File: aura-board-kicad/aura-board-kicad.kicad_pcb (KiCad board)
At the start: 2 copper layers, 75.6 x 53.3 mm, 16 parts, among them J1 Main Power, J2 PWM Outputs, J3 BB-UART0, J4 Attopilot, J5 GPS, J6 SBUS, J7 Telemetry, U1 TSR2-2450, U2 PocketBeagle, U3 Teensy-3.2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

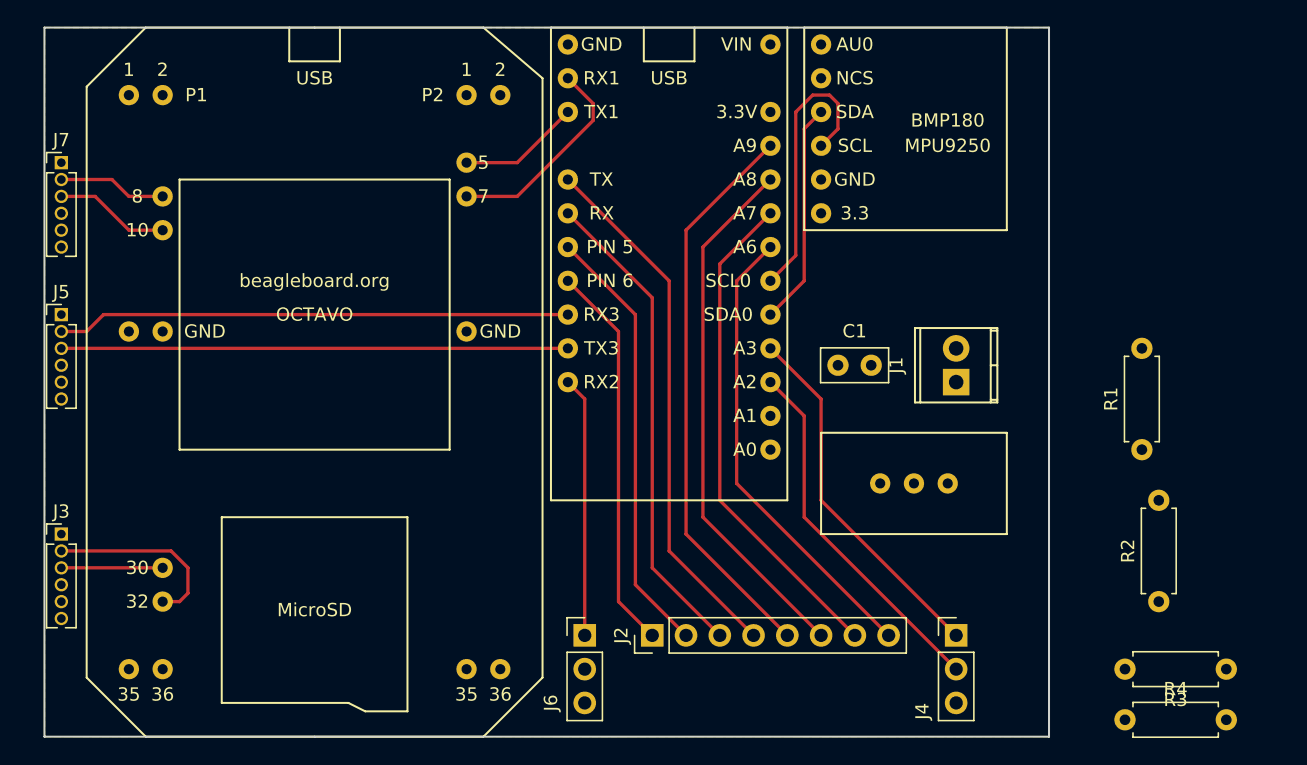
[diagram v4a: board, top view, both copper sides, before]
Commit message: More trace routing and tweaking.
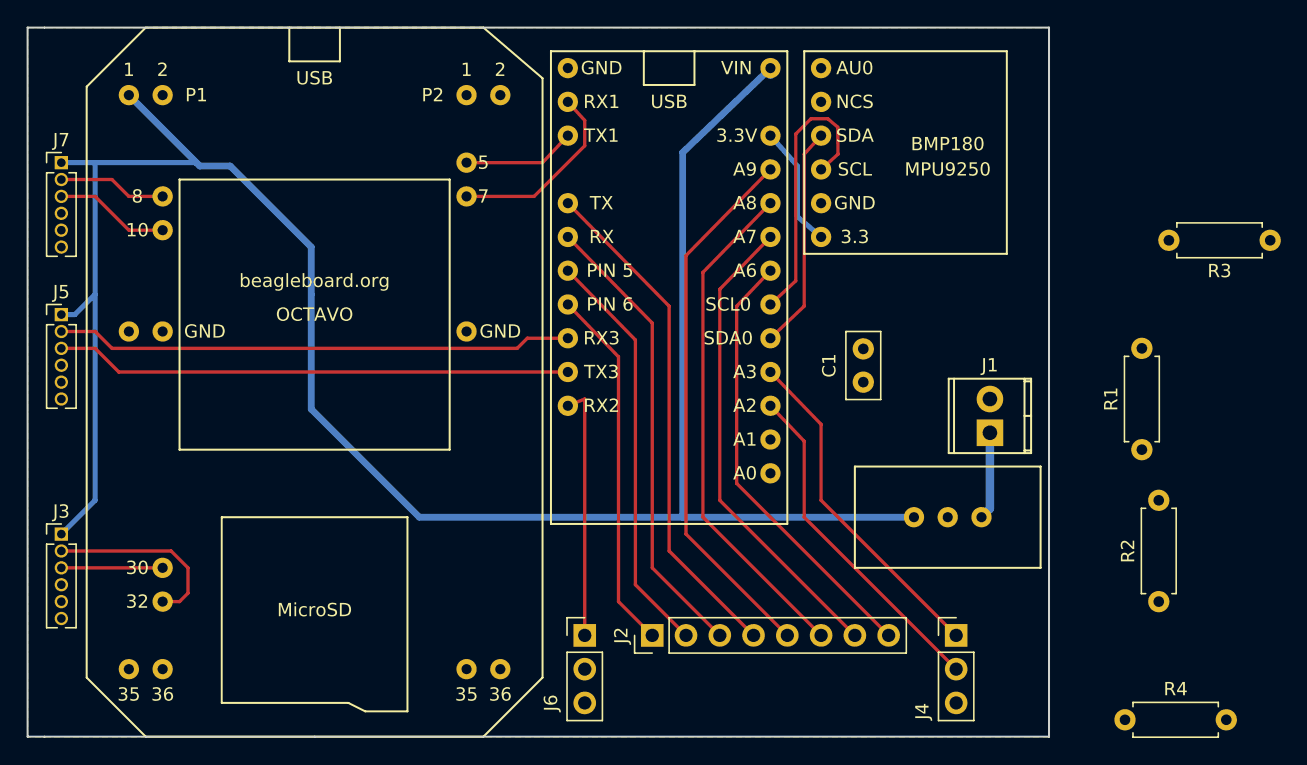
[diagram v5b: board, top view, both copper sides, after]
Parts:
- moved R3 32.4 mm to (121.4, 65.5)
- moved J1 4.58 mm to (100.3, 80.0)
- moved U1 3.59 mm to (97.2, 90.2)
- moved C1 2.29 mm to (90.8, 76.2), turned to 90 degrees
- moved U4 1.78 mm to (94.0, 66.5)
- moved U3 1.78 mm to (76.2, 51.3)
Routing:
- net +5V: track 0.00 -> 158.9 mm
- net +3V3: track 0.00 -> 9.21 mm
- net VDD: track 0.00 -> 6.61 mm
- net /PWM4: track 40.1 -> 38.3 mm
- net /PWM3: track 36.5 -> 34.7 mm
- net /PWM5: track 42.6 -> 40.8 mm
- net /PWM2: track 32.9 -> 31.1 mm
- net /PWM6: track 40.1 -> 38.3 mm
- net /PWM7: track 37.5 -> 35.7 mm
- net /PWM1: track 29.3 -> 27.5 mm
- net /ATTO_VOLTS: track 27.4 -> 25.6 mm
- net /PWM8: track 35.0 -> 33.2 mm
- net /ATTO_AMPS: track 27.4 -> 25.6 mm
- net /UART1_RX: track 15.9 -> 14.3 mm
- net /GPS_TX: track 38.1 -> 38.8 mm
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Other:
- board size 75.6 x 53.3 mm -> 76.8 x 53.3 mm

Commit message: More trace routing. Position resistors for voltage divider/sending circuits. Add mounting holes (3mm).
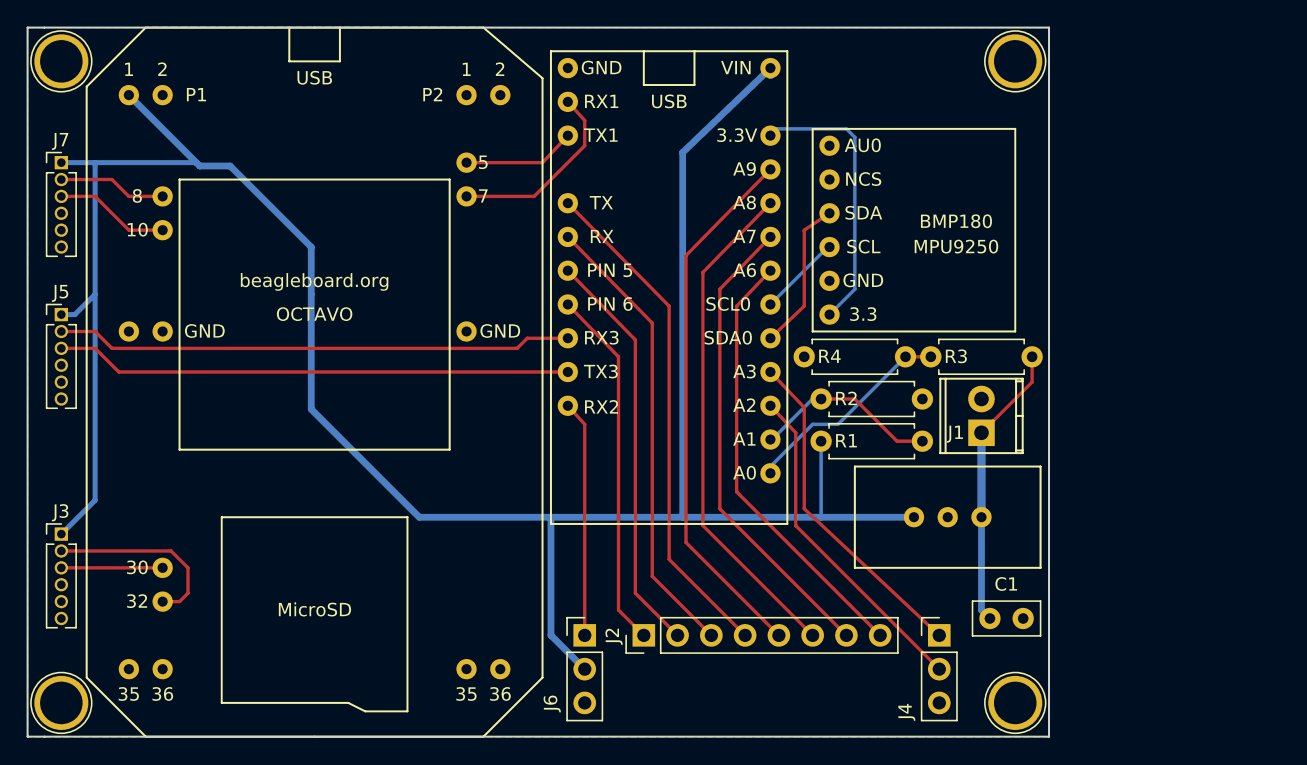
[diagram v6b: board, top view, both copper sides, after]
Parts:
- added REF**: 1pin, Connectors:1pin, F.Cu at (30.5, 52.1)
- added REF**: 1pin, Connectors:1pin, F.Cu at (30.5, 100.3)
- added REF**: 1pin, Connectors:1pin, F.Cu at (102.2, 100.3)
- added REF**: 1pin, Connectors:1pin, F.Cu at (102.2, 52.1)
- moved R4 36.4 mm to (86.4, 74.3)
- moved R3 27.0 mm to (95.9, 74.3), turned to 0 degrees
- moved R2 23.4 mm to (95.2, 77.5), turned to 180 degrees
- moved C1 20.2 mm to (100.3, 94.0), turned to 0 degrees
- moved R1 16.5 mm to (95.2, 80.6), turned to 180 degrees
- moved U4 5.88 mm to (94.6, 72.4)
- moved J4 1.27 mm to (96.5, 95.2)
- moved J1 0.64 mm to (99.7, 80.0)
- moved J2 0.64 mm to (74.3, 95.2)
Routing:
- net +5V: track 158.9 -> 176.5 mm
- net /MAIN_VCC: track 0.00 -> 16.0 mm
- net /I2C0_SCL: track 21.3 -> 6.23 mm
- net VDD: track 6.61 -> 21.5 mm
- net /AVIONICS_VCC: track 0.00 -> 14.0 mm
- net +3V3: track 9.21 -> 20.9 mm
- net /I2C0_SDA: track 16.8 -> 11.5 mm
- net /SBUS_RX: track 19.1 -> 17.8 mm
- net /ATTO_AMPS: track 25.6 -> 25.0 mm

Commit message: Add a +5V power bus plane on the top layer.
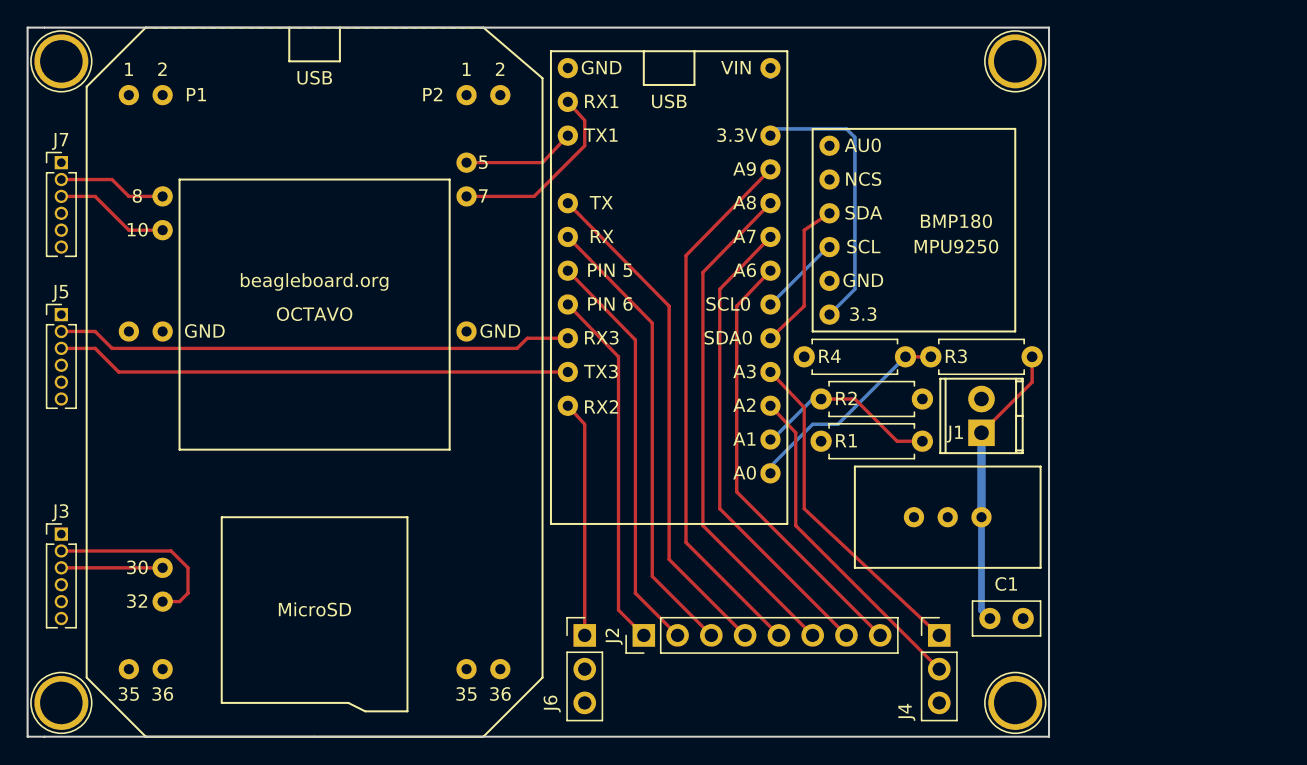
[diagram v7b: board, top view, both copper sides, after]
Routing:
- net +5V: track 176.5 -> 1.02 mm
- added copper zone on F.Cu, net +5V

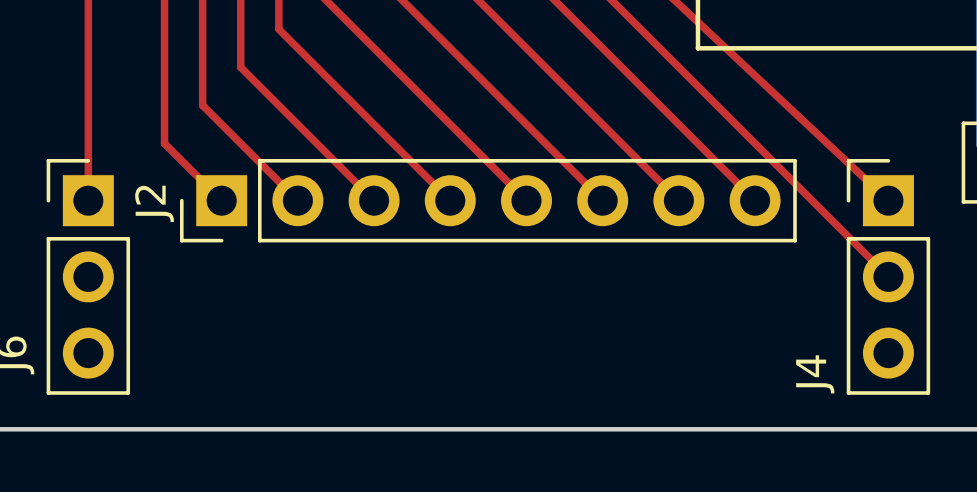
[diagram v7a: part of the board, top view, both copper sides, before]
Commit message: Add pin headers to complete pwm header block.
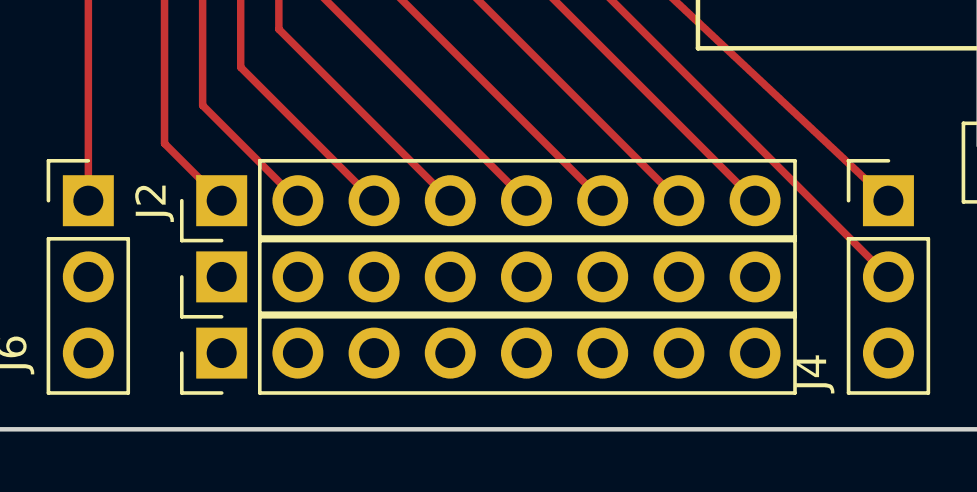
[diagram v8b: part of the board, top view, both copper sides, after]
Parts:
- added ?: 1x08, Pin_Headers:Pin_Header_Straight_1x08_Pitch2.54mm, F.Cu at (74.3, 97.8)
- added ?: 1x08, Pin_Headers:Pin_Header_Straight_1x08_Pitch2.54mm, F.Cu at (74.3, 100.3)
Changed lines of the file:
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@@
     (tracks 92)
     (zones 0)
-    (modules 20)
+    (modules 22)
     (nets 33)
   )
@@
   (layers
     (0 F.Cu signal)
-    (31 B.Cu signal hide)
+    (31 B.Cu signal)
     (32 B.Adhes user)
     (33 F.Adhes user)
@@
     (fp_line (start 1.8 19.55) (end 1.8 -1.8) (layer F.CrtYd) (width 0.05))
     (fp_line (start 1.8 -1.8) (end -1.8 -1.8) (layer F.CrtYd) (width 0.05))
-    (fp_text user %R (at 0 8.89 180) (layer F.Fab)
+    (fp_text user %R (at 2.54 -0.635 180) (layer F.Fab)
       (effects (font (size 1 1) (thickness 0.15)))
     )
@@
     (fp_line (start 1.8 6.85) (end 1.8 -1.8) (layer F.CrtYd) (width 0.05))
     (fp_line (start 1.8 -1.8) (end -1.8 -1.8) (layer F.CrtYd) (width 0.05))
-    (fp_text user %R (at 0 2.54 90) (layer F.Fab)
+    (fp_text user %R (at -1.905 2.54 90) (layer F.Fab)
       (effects (font (size 1 1) (thickness 0.15)))
     )
@@
     (pad 1 thru_hole circle (at 0 0) (size 4.064 4.064) (drill 3.2) (layers *.Cu *.Mask))
   )
+  (module Pin_Headers:Pin_Header_Straight_1x08_Pitch2.54mm (layer F.Cu)
+    (at 74.295 97.79 90)
+    (descr "Through hole straight pin header, 1x08, 2.54mm pitch, single row")
+    (tags "Through hole pin header THT 1x08 2.54mm single row")
+    (fp_text reference "" (at 0 -2.33 90) (layer F.SilkS) hide
+      (effects (font (size 1 1) (thickness 0.15)))
+    )
+    (fp_text value 1x08 (at 0 20.11 90) (layer F.Fab) hide
+      (effects (font (size 1 1) (thickness 0.15)))
+    )
+    (fp_line (start -0.635 -1.27) (end 1.27 -1.27) (layer F.Fab) (width 0.1))
+    (fp_line (start 1.27 -1.27) (end 1.27 19.05) (layer F.Fab) (width 0.1))
+    (fp_line (start 1.27 19.05) (end -1.27 19.05) (layer F.Fab) (width 0.1))
+    (fp_line (start -1.27 19.05) (end -1.27 -0.635) (layer F.Fab) (width 0.1))
+    (fp_line (start -1.27 -0.635) (end -0.635 -1.27) (layer F.Fab) (width 0.1))
+    (fp_line (start -1.33 19.11) (end 1.33 19.11) (layer F.SilkS) (width 0.12))
+    (fp_line (start -1.33 1.27) (end -1.33 19.11) (layer F.SilkS) (width 0.12))
+    (fp_line (start 1.33 1.27) (end 1.33 19.11) (layer F.SilkS) (width 0.12))
+    (fp_line (start -1.33 1.27) (end 1.33 1.27) (layer F.SilkS) (width 0.12))
+    (fp_line (start -1.33 0) (end -1.33 -1.33) (layer F.SilkS) (width 0.12))
+    (fp_line (start -1.33 -1.33) (end 0 -1.33) (layer F.SilkS) (width 0.12))
+    (fp_line (start -1.8 -1.8) (end -1.8 19.55) (layer F.CrtYd) (width 0.05))
+    (fp_line (start -1.8 19.55) (end 1.8 19.55) (layer F.CrtYd) (width 0.05))
+    (fp_line (start 1.8 19.55) (end 1.8 -1.8) (layer F.CrtYd) (width 0.05))
+    (fp_line (start 1.8 -1.8) (end -1.8 -1.8) (layer F.CrtYd) (width 0.05))
+    (fp_text user %R (at 0 8.89 180) (layer F.Fab) hide
+      (effects (font (size 1 1) (thickness 0.15)))
+    )
+    (pad 1 thru_hole rect (at 0 0 90) (size 1.7 1.7) (drill 1) (layers *.Cu *.Mask))
+    (pad 2 thru_hole oval (at 0 2.54 90) (size 1.7 1.7) (drill 1) (layers *.Cu *.Mask))
+    (pad 3 thru_hole oval (at 0 5.08 90) (size 1.7 1.7) (drill 1) (layers *.Cu *.Mask))
+    (pad 4 thru_hole oval (at 0 7.62 90) (size 1.7 1.7) (drill 1) (layers *.Cu *.Mask))
+    (pad 5 thru_hole oval (at 0 10.16 90) (size 1.7 1.7) (drill 1) (layers *.Cu *.Mask))
+    (pad 6 thru_hole oval (at 0 12.7 90) (size 1.7 1.7) (drill 1) (layers *.Cu *.Mask))
+    (pad 7 thru_hole oval (at 0 15.24 90) (size 1.7 1.7) (drill 1) (layers *.Cu *.Mask))
+    (pad 8 thru_hole oval (at 0 17.78 90) (size 1.7 1.7) (drill 1) (layers *.Cu *.Mask))
+    (model ${KISYS3DMOD}/Pin_Headers.3dshapes/Pin_Header_Straight_1x08_Pitch2.54mm.wrl
+      (at (xyz 0 0 0))
+      (scale (xyz 1 1 1))
+      (rotate (xyz 0 0 0))
+    )
+  )
+  (module Pin_Headers:Pin_Header_Straight_1x08_Pitch2.54mm (layer F.Cu)
+    (at 74.295 100.33 90)
+    (descr "Through hole straight pin header, 1x08, 2.54mm pitch, single row")
+    (tags "Through hole pin header THT 1x08 2.54mm single row")
+    (fp_text reference "" (at 0 -2.33 90) (layer F.SilkS) hide
+      (effects (font (size 1 1) (thickness 0.15)))
+    )
+    (fp_text value 1x08 (at 0 20.11 90) (layer F.Fab) hide
+      (effects (font (size 1 1) (thickness 0.15)))
+    )
+    (fp_line (start -0.635 -1.27) (end 1.27 -1.27) (layer F.Fab) (width 0.1))
+    (fp_line (start 1.27 -1.27) (end 1.27 19.05) (layer F.Fab) (width 0.1))
+    (fp_line (start 1.27 19.05) (end -1.27 19.05) (layer F.Fab) (width 0.1))
+    (fp_line (start -1.27 19.05) (end -1.27 -0.635) (layer F.Fab) (width 0.1))
+    (fp_line (start -1.27 -0.635) (end -0.635 -1.27) (layer F.Fab) (width 0.1))
+    (fp_line (start -1.33 19.11) (end 1.33 19.11) (layer F.SilkS) (width 0.12))
+    (fp_line (start -1.33 1.27) (end -1.33 19.11) (layer F.SilkS) (width 0.12))
+    (fp_line (start 1.33 1.27) (end 1.33 19.11) (layer F.SilkS) (width 0.12))
+    (fp_line (start -1.33 1.27) (end 1.33 1.27) (layer F.SilkS) (width 0.12))
+    (fp_line (start -1.33 0) (end -1.33 -1.33) (layer F.SilkS) (width 0.12))
+    (fp_line (start -1.33 -1.33) (end 0 -1.33) (layer F.SilkS) (width 0.12))
+    (fp_line (start -1.8 -1.8) (end -1.8 19.55) (layer F.CrtYd) (width 0.05))
+    (fp_line (start -1.8 19.55) (end 1.8 19.55) (layer F.CrtYd) (width 0.05))
+    (fp_line (start 1.8 19.55) (end 1.8 -1.8) (layer F.CrtYd) (width 0.05))
+    (fp_line (start 1.8 -1.8) (end -1.8 -1.8) (layer F.CrtYd) (width 0.05))
+    (fp_text user %R (at 0 8.89 180) (layer F.Fab) hide
+      (effects (font (size 1 1) (thickness 0.15)))
+    )
+    (pad 1 thru_hole rect (at 0 0 90) (size 1.7 1.7) (drill 1) (layers *.Cu *.Mask))
+    (pad 2 thru_hole oval (at 0 2.54 90) (size 1.7 1.7) (drill 1) (layers *.Cu *.Mask))
+    (pad 3 thru_hole oval (at 0 5.08 90) (size 1.7 1.7) (drill 1) (layers *.Cu *.Mask))
+    (pad 4 thru_hole oval (at 0 7.62 90) (size 1.7 1.7) (drill 1) (layers *.Cu *.Mask))
+    (pad 5 thru_hole oval (at 0 10.16 90) (size 1.7 1.7) (drill 1) (layers *.Cu *.Mask))
+    (pad 6 thru_hole oval (at 0 12.7 90) (size 1.7 1.7) (drill 1) (layers *.Cu *.Mask))
+    (pad 7 thru_hole oval (at 0 15.24 90) (size 1.7 1.7) (drill 1) (layers *.Cu *.Mask))
+    (pad 8 thru_hole oval (at 0 17.78 90) (size 1.7 1.7) (drill 1) (layers *.Cu *.Mask))
+    (model ${KISYS3DMOD}/Pin_Headers.3dshapes/Pin_Header_Straight_1x08_Pitch2.54mm.wrl
+      (at (xyz 0 0 0))
+      (scale (xyz 1 1 1))
+      (rotate (xyz 0 0 0))
+    )
+  )
   (gr_line (start 29.21 49.53) (end 27.94 49.53) (angle 90) (layer Edge.Cuts) (width 0.15))
